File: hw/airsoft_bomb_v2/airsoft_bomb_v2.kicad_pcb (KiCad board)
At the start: 2 copper layers, 71.4 x 76.7 mm, 52 parts, among them J1 Conn_01x10_Pin, J2 Conn_01x16_Pin, J3 BTN_R, J4 BTN_Y, J5 SIREN, J6 Conn_01x02_Socket, Q2 AO3400A, Q4 AO3400A, Q5 AO3400A, U1 PCF8574, U2 PCF8574, U4 LM317_SOT-223

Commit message: mark creen/keypad connectors on other side of pcb mark siren +/-
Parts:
- added kibuzzard-687FD9CC: G***, kibuzzard-687FD9CC, B.Cu at (119.1, 82.0)
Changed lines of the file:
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@@
 		)
 	)
+	(footprint "kibuzzard-687FD9CC"
+		(layer "B.Cu")
+		(at 119.126 82.042 90)
+		(descr "Generated with KiBuzzard")
+		(tags "kb_params=eyJBbGlnbm1lbnRDaG9pY2UiOiAiQ2VudGVyIiwgIkNhcExlZnRDaG9pY2UiOiAiPCIsICJDYXBSaWdodENob2ljZSI6ICI+IiwgIkZvbnRDb21ib0JveCI6ICJVYnVudHVNb25vLUIiLCAiSGVpZ2h0Q3RybCI6IDEuMCwgIkxheWVyQ29tYm9Cb3giOiAiRi5TaWxrUyIsICJMaW5lU3BhY2luZ0N0cmwiOiAxLjUsICJNdWx0aUxpbmVUZXh0IjogIisgICAgLSIsICJQYWRkaW5nQm90dG9tQ3RybCI6IDIuMCwgIlBhZGRpbmdMZWZ0Q3RybCI6IDIuMCwgIlBhZGRpbmdSaWdodEN0cmwiOiAyLjAsICJQYWRkaW5nVG9wQ3RybCI6IDIuMCwgIldpZHRoQ3RybCI6IDUuMCwgImFkdmFuY2VkQ2hlY2tib3giOiBmYWxzZSwgImlubGluZUZvcm1hdFRleHRib3giOiBmYWxzZSwgImxpbmVvdmVyU3R5bGVDaG9pY2UiOiAiU3F1YXJlIiwgImxpbmVvdmVyVGhpY2tuZXNzQ3RybCI6IDF9")
+		(property "Reference" "kibuzzard-687FD9CC"
+			(at 0 3.679933 90)
+			(layer "B.SilkS")
+			(hide yes)
+			(effects
+				(font
+					(size 0.001 0.001)
+				)
+				(justify mirror)
+			)
+		)
+		(property "Value" "G***"
+			(at 0 -3.679933 90)
+			(layer "B.SilkS")
+			(hide yes)
+			(effects
+				(font
+					(size 0.001 0.001)
+				)
+				(justify mirror)
+			)
+		)
+		(property "Footprint" ""
+			(at 0 0 90)
+			(layer "B.Fab")
+			(hide yes)
+			(effects
+				(font
+					(size 1.27 1.27)
+					(thickness 0.15)
+				)
+				(justify mirror)
+			)
+		)
+		(property "Datasheet" ""
+			(at 0 0 90)
+			(layer "B.Fab")
+			(hide yes)
+			(effects
+				(font
+					(size 1.27 1.27)
+					(thickness 0.15)
+				)
+				(justify mirror)
+			)
+		)
+		(property "Description" ""
+			(at 0 0 90)
+			(layer "B.Fab")
+			(hide yes)
+			(effects
+				(font
+					(size 1.27 1.27)
+					(thickness 0.15)
+				)
+				(justify mirror)
+			)
+		)
+		(attr board_only exclude_from_pos_files exclude_from_bom)
+		(fp_poly
+			(pts
+				(xy -2.299677 0.631933) (xy -2.568928 0.631933) (xy -2.990217 0) (xy -2.568928 -0.631933) (xy -2.299677 -0.631933)
+				(xy -1.874798 -0.631933) (xy -1.874798 -0.362682) (xy -2.046042 -0.362682) (xy -2.046042 -0.081583)
+				(xy -2.299677 -0.081583) (xy -2.299677 0.081583) (xy -2.046042 0.081583) (xy -2.046042 0.362682)
+				(xy -1.874798 0.362682) (xy -1.874798 0.081583) (xy -1.621163 0.081583) (xy -1.621163 -0.081583)
+				(xy -1.874798 -0.081583) (xy -1.874798 -0.362682) (xy -1.874798 -0.631933) (xy 2.299677 -0.631933)
+				(xy 2.299677 -0.107431) (xy 1.857027 -0.107431) (xy 1.857027 0.088045) (xy 2.299677 0.088045) (xy 2.299677 -0.107431)
+				(xy 2.299677 -0.631933) (xy 2.568928 -0.631933) (xy 2.990217 0) (xy 2.568928 0.631933) (xy 2.299677 0.631933)
+				(xy -2.299677 0.631933)
+			)
+			(stroke
+				(width 0)
+				(type solid)
+			)
+			(fill solid)
+			(layer "B.SilkS")
+		)
+	)
 	(footprint "Resistor_SMD:R_0805_2012Metric_Pad1.20x1.40mm_HandSolder"
 		(layer "B.Cu")
@@
 		)
 	)
+	(gr_rect
+		(start 175.768 125.476)
+		(end 178.308 134.112)
+		(stroke
+			(width 0.1)
+			(type default)
+		)
+		(fill solid)
+		(layer "B.SilkS")
+	)
+	(gr_rect
+		(start 152.908 125.476)
+		(end 155.448 134.112)
+		(stroke
+			(width 0.1)
+			(type default)
+		)
+		(fill solid)
+		(layer "B.SilkS")
+	)
+	(gr_rect
+		(start 170.18 58.928)
+		(end 172.72 67.564)
+		(stroke
+			(width 0.1)
+			(type default)
+		)
+		(fill solid)
+		(layer "B.SilkS")
+	)
+	(gr_rect
+		(start 132.08 58.928)
+		(end 134.62 67.564)
+		(stroke
+			(width 0.1)
+			(type default)
+		)
+		(fill solid)
+		(layer "B.SilkS")
+	)
 	(gr_line

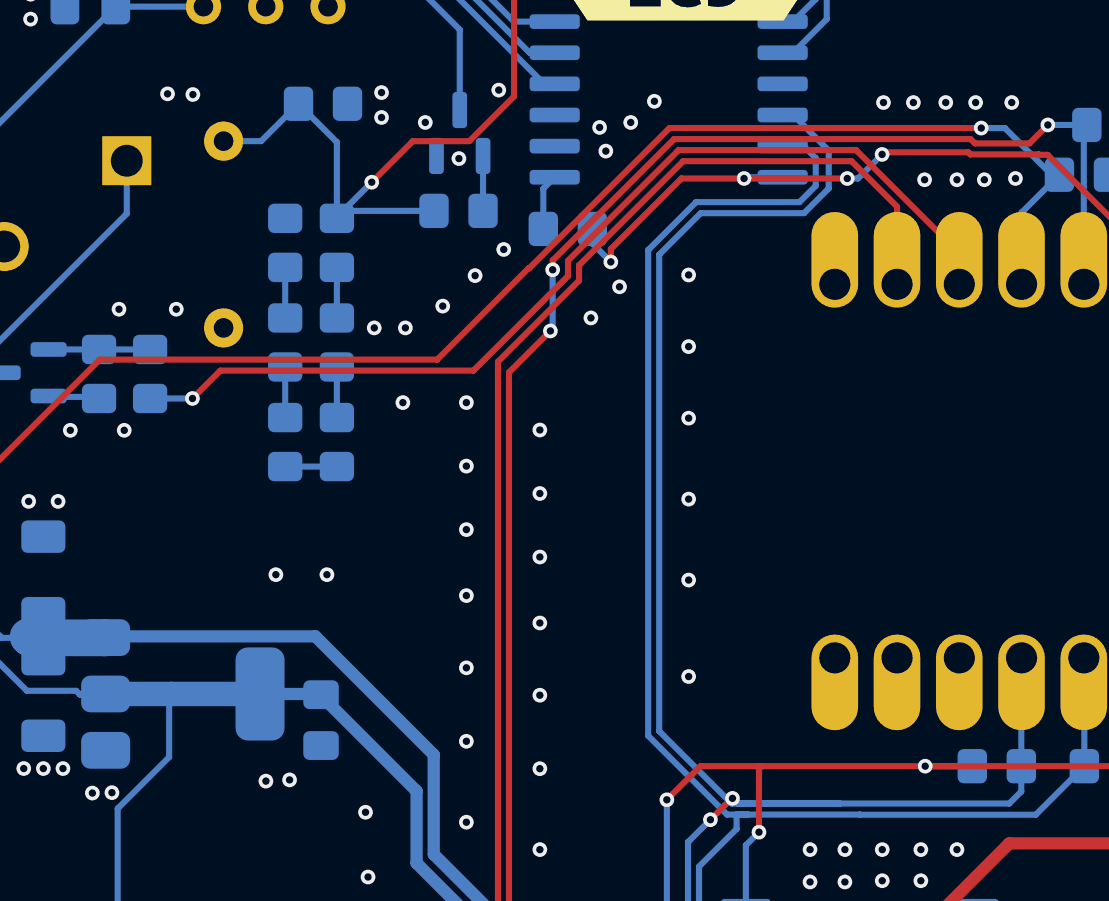
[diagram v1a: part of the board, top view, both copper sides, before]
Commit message: move siren pin to something that is not high on boot
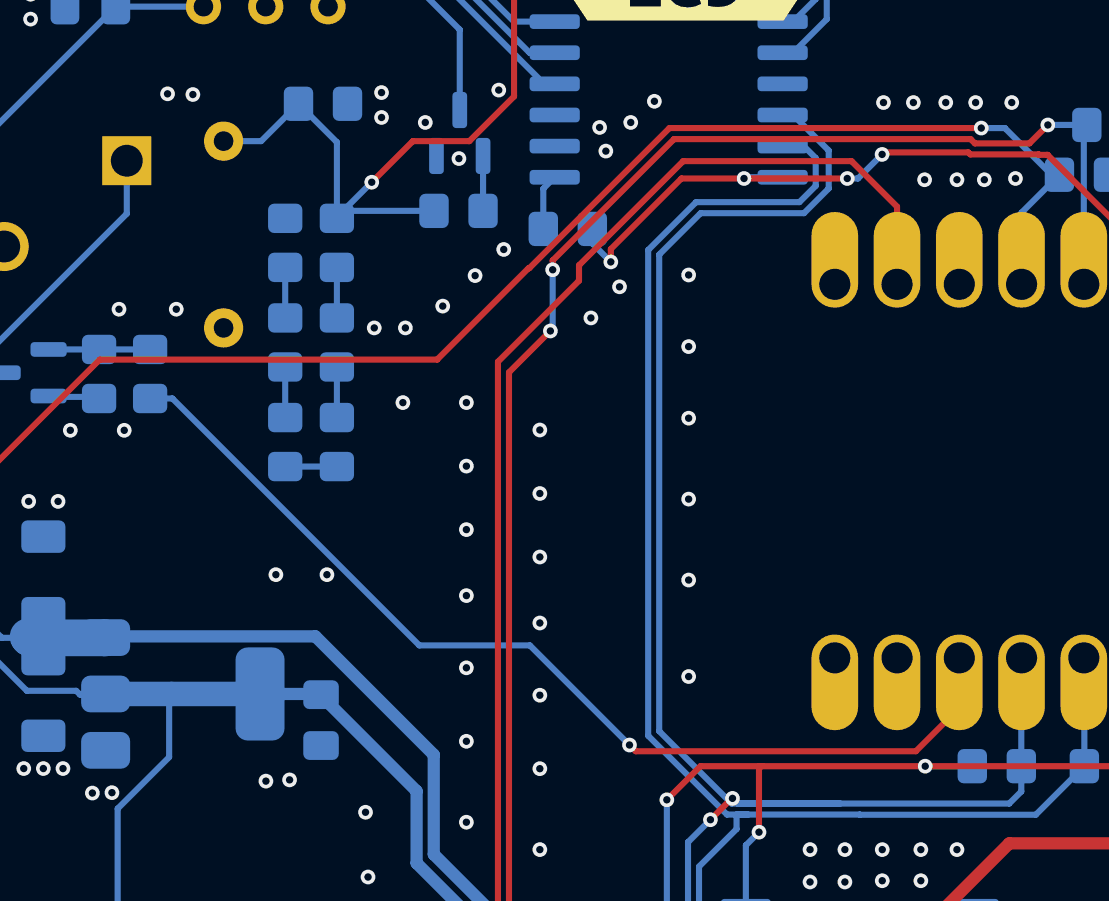
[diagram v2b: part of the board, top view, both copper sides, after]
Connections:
- R9 pad 2: Net-(U3-GPIO2) -> Net-(U3-GPIO10)
- U3 pad 10: unconnected-(U3-GPIO10-Pad10) -> Net-(U3-GPIO10)
- U3 pad 2: Net-(U3-GPIO2) -> unconnected-(U3-GPIO2-Pad2)
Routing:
- net Net-(U3-GPIO10): track 0.00 -> 41.7 mm, vias 0 -> 1
- net Net-(U3-GPIO2): track 39.3 -> 0.00 mm, vias 1 -> 0
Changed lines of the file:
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@@
 	(net 35 "/I2C_SCL")
 	(net 36 "Net-(U3-GPIO1)")
-	(net 37 "Net-(U3-GPIO2)")
+	(net 37 "Net-(U3-GPIO10)")
 	(net 38 "Net-(R12-Pad2)")
 	(net 39 "Net-(R12-Pad1)")
@@
 	(net 43 "unconnected-(U2-~{INT}-Pad13)")
 	(net 44 "unconnected-(U3-GPIO21-Pad21)")
-	(net 45 "unconnected-(U3-GPIO10-Pad10)")
+	(net 45 "unconnected-(U3-GPIO2-Pad2)")
 	(net 46 "unconnected-(U3-GPIO20-Pad20)")
 	(net 47 "unconnected-(U3-GPIO7-Pad7)")
@@
 				(font
 					(size 0.001 0.001)
+					(thickness 0.15)
 				)
 				(justify mirror)
@@
 				(font
 					(size 0.001 0.001)
+					(thickness 0.15)
 				)
 				(justify mirror)
@@
 			)
 			(remove_unused_layers no)
-			(net 37 "Net-(U3-GPIO2)")
+			(net 45 "unconnected-(U3-GPIO2-Pad2)")
 			(pinfunction "GPIO2")
-			(pintype "bidirectional")
+			(pintype "bidirectional+no_connect")
 			(solder_mask_margin 0.1016)
 			(thermal_bridge_angle 0)
@@
 			)
 			(remove_unused_layers no)
-			(net 45 "unconnected-(U3-GPIO10-Pad10)")
+			(net 37 "Net-(U3-GPIO10)")
 			(pinfunction "GPIO10")
-			(pintype "bidirectional+no_connect")
+			(pintype "bidirectional")
 			(solder_mask_margin 0.1016)
 			(thermal_bridge_angle 0)
@@
 			(layers "B.Cu" "B.Paste" "B.Mask")
 			(roundrect_rratio 0.208333)
-			(net 37 "Net-(U3-GPIO2)")
+			(net 37 "Net-(U3-GPIO10)")
 			(pintype "passive")
 		)
@@
 	)
 	(segment
-		(start 132.2832 90.0016)
-		(end 133.4202 88.8646)
+		(start 161.798 104.394)
+		(end 163.57 102.622)
 		(width 0.25)
 		(layer "F.Cu")
@@
 	)
 	(segment
-		(start 159.361258 79.8686)
-		(end 163.57 84.077342)
+		(start 150.114 104.14)
+		(end 150.368 104.394)
 		(width 0.25)
 		(layer "F.Cu")
@@
 	)
 	(segment
-		(start 147.604658 85.008542)
-		(end 147.604658 84.38145)
+		(start 163.57 102.622)
+		(end 163.57 100.584)
 		(width 0.25)
 		(layer "F.Cu")
@@
 	)
 	(segment
-		(start 143.7486 88.8646)
-		(end 147.604658 85.008542)
+		(start 150.368 104.394)
+		(end 161.798 104.394)
 		(width 0.25)
 		(layer "F.Cu")
 		(net 37)
 	)
-	(segment
-		(start 133.4202 88.8646)
-		(end 143.7486 88.8646)
-		(width 0.25)
-		(layer "F.Cu")
+	(via
+		(at 150.114 104.14)
+		(size 0.6)
+		(drill 0.3)
+		(layers "F.Cu" "B.Cu")
 		(net 37)
 	)
 	(segment
-		(start 152.117508 79.8686)
-		(end 159.361258 79.8686)
+		(start 146.05 100.076)
+		(end 150.114 104.14)
 		(width 0.25)
-		(layer "F.Cu")
+		(layer "B.Cu")
 		(net 37)
 	)
 	(segment
-		(start 147.604658 84.38145)
-		(end 152.117508 79.8686)
+		(start 130.556 90.0016)
+		(end 131.465284 90.0016)
 		(width 0.25)
-		(layer "F.Cu")
+		(layer "B.Cu")
 		(net 37)
 	)
-	(via
-		(at 132.2832 90.0016)
-		(size 0.6)
-		(drill 0.3)
-		(layers "F.Cu" "B.Cu")
+	(segment
+		(start 131.465284 90.0016)
+		(end 141.539684 100.076)
+		(width 0.25)
+		(layer "B.Cu")
 		(net 37)
 	)
 	(segment
-		(start 132.2832 90.0016)
-		(end 130.556 90.0016)
+		(start 141.539684 100.076)
+		(end 146.05 100.076)
 		(width 0.25)
 		(layer "B.Cu")

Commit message: version silkscreen
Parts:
- removed kibuzzard-67B9068C: G***, kibuzzard-67B9068C
- added kibuzzard-68963AB1: G***, kibuzzard-68963AB1, B.Cu at (168.7, 74.7)

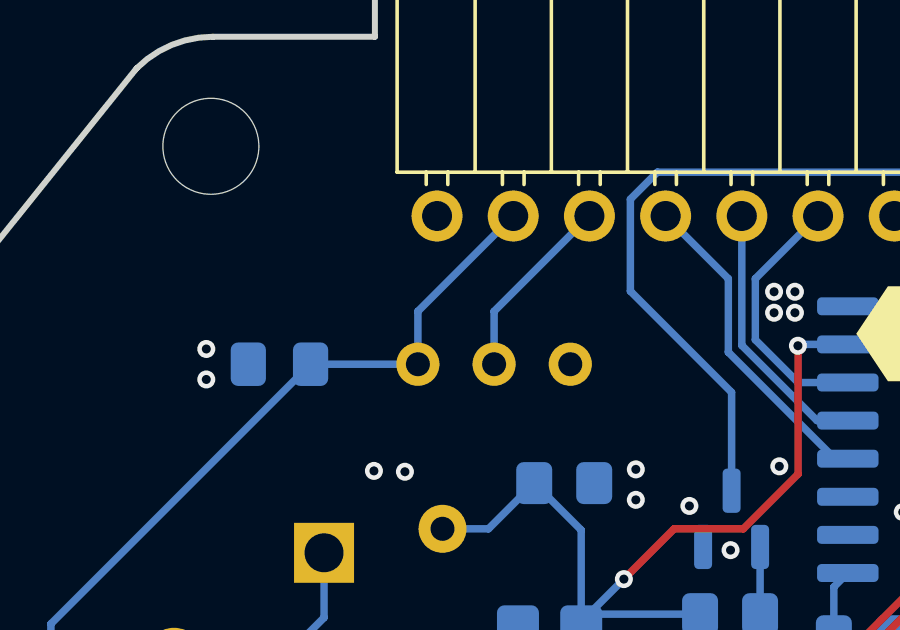
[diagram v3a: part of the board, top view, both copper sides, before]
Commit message: change potentiometer to smd
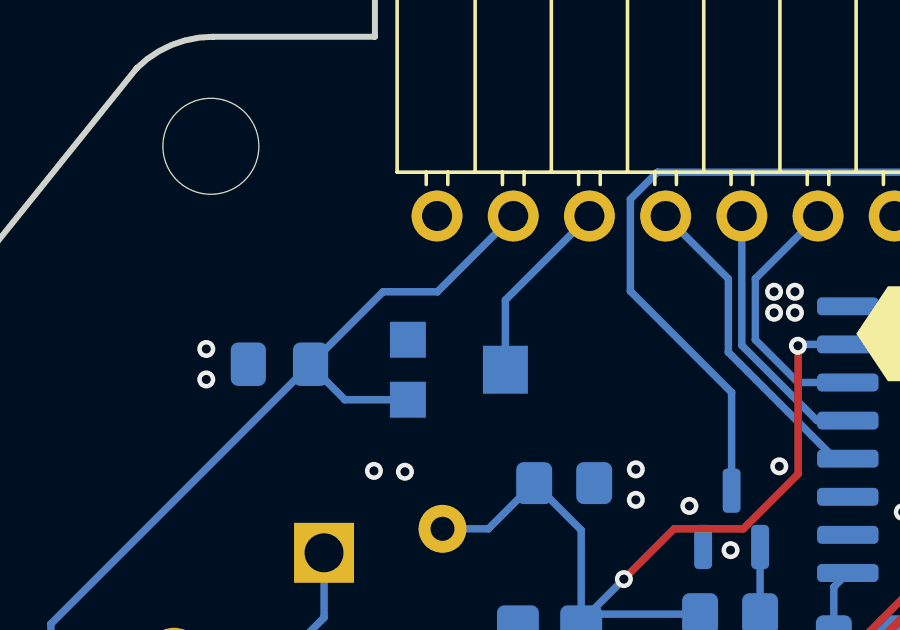
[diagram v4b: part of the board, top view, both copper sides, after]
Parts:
- RV1: footprint Potentiometer_THT:Potentiometer_Bourns_3296W_Vertical -> !custom:Potentiometer_Bourns_TC33X_Vertical
- moved RV1 1.48 mm to (134.2, 74.2), turned to 0 degrees
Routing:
- net +5V: track 169.6 -> 172.4 mm

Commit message: add polarity protection diode on voltage input lcsc part numbers
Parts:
- added D1: D, Diode_SMD:D_SOD-123, B.Cu at (132.0, 97.0)
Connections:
- J6 pad 2: VCC -> Net-(D1-A)
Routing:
- net VCC: track 80.1 -> 28.2 mm, vias 1 -> 0
- net Net-(D1-A): track 0.00 -> 51.6 mm, vias 0 -> 1
